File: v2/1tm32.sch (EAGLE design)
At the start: 48 parts, among them IC1 STM32L412RBT6P, IC2 BGM240PA32VNN3, IC3 TPS7A0333PYCHR, J2 10118192-0001LF, J3 FTSH-105-01-L-D, J4 20021321-00020C4LF, SW1 LL3301FF065QJ, U2 LD39050PU33R, Y1 8MHz, Y2 32.7KHz

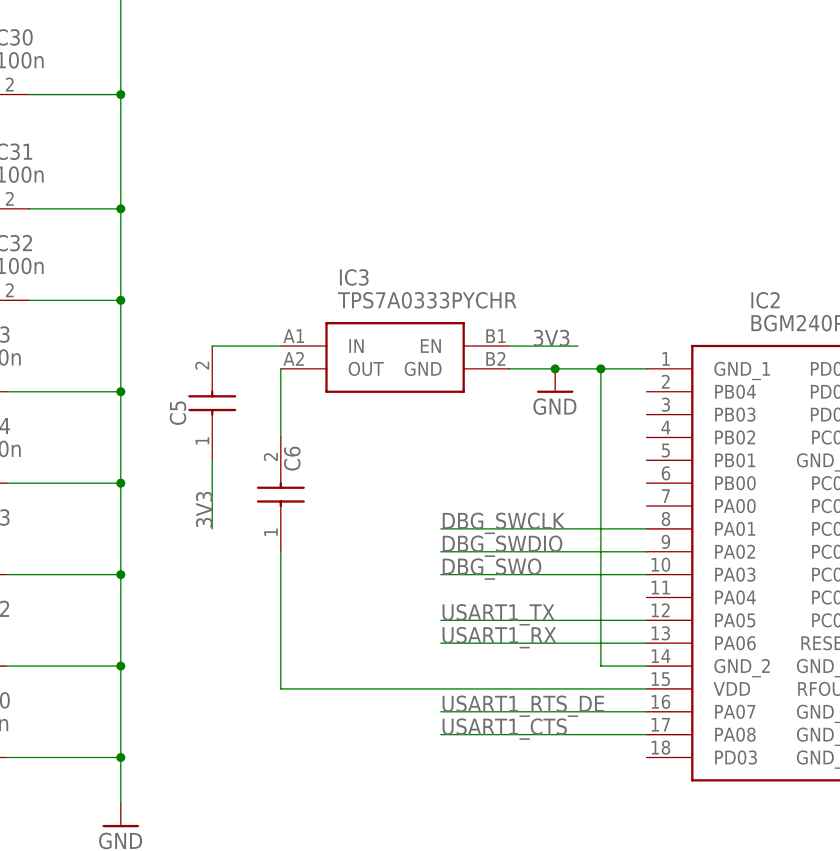
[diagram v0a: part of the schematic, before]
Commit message: changed voltage regulator
previous one caused clearance issues with the wires
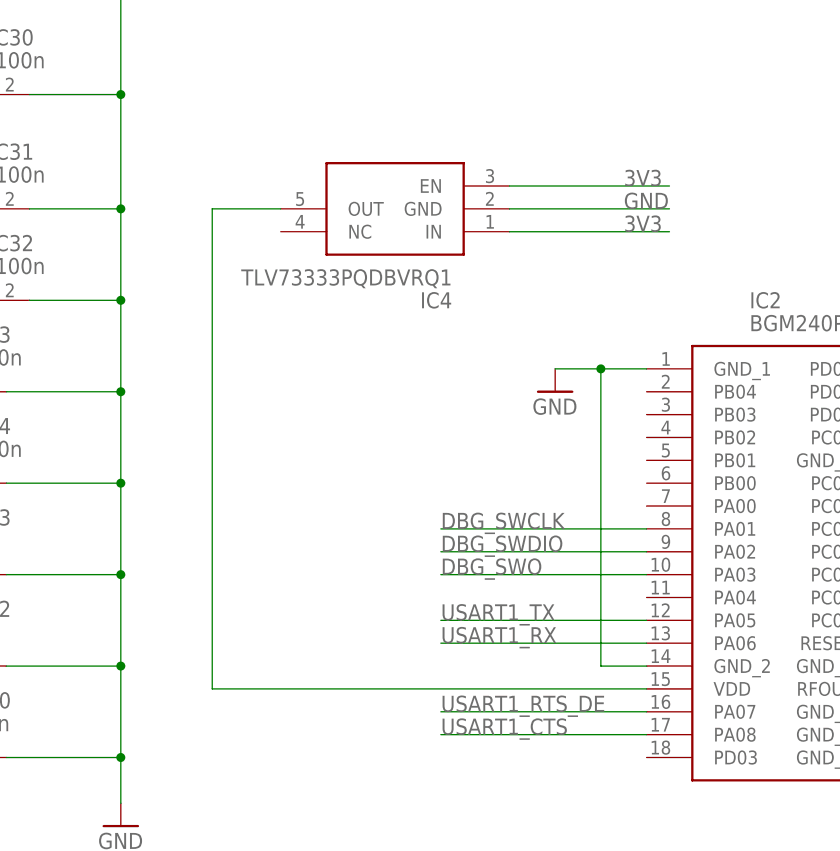
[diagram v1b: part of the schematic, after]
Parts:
- removed C5, C6: GRM219R61H105KA73D, GRM219R61H105KA73D(1u):GRM219R61H105KA73D
- removed IC3: TPS7A0333PYCHR, TPS7A0333PYCHR(volt_reg):TPS7A0333PYCHR
- added IC4: TLV73333PQDBVRQ1, TLV73333PQDBVRQ1(volt_reg2):TLV73333PQDBVRQ1
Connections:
- removed net N$1: C6.2, IC3.OUT
- removed net N$6: C5.2, IC3.IN
- net 3V3: now also IC4.EN, IC4.IN; no longer C5.1, IC3.EN
- net GND: now also IC4.GND; no longer IC3.GND
- net N$4: now also IC4.OUT; no longer C6.1
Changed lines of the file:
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@@
 <part name="R11" library="RC0805JR-0710KL" deviceset="RC0805JR-0710KL" device="" value="10K"/>
 <part name="U$2" library="RBR1L30ATE25(scho_diode)" deviceset="RBR1L30ATE25" device=""/>
-<part name="IC3" library="TPS7A0333PYCHR(volt_reg)" deviceset="TPS7A0333PYCHR" device=""/>
-<part name="C5" library="GRM219R61H105KA73D(1u)" deviceset="GRM219R61H105KA73D" device=""/>
-<part name="C6" library="GRM219R61H105KA73D(1u)" deviceset="GRM219R61H105KA73D" device=""/>
+<part name="IC4" library="TLV73333PQDBVRQ1(volt_reg2)" deviceset="TLV73333PQDBVRQ1" device=""/>
 </parts>
 <sheets>
@@
 <attribute name="VALUE" x="-150.1394" y="138.6586" size="2.0828" layer="96" ratio="6" rot="SR0"/>
 </instance>
-<instance part="IC3" gate="G$1" x="-73.66" y="-45.72" smashed="yes">
-<attribute name="NAME" x="-67.31" y="-38.1" size="1.778" layer="95" align="center-left"/>
-<attribute name="VALUE" x="-67.31" y="-40.64" size="1.778" layer="96" align="center-left"/>
-</instance>
-<instance part="C5" gate="G$1" x="-81.28" y="-58.42" smashed="yes" rot="R90">
-<attribute name="NAME" x="-85.09" y="-54.61" size="1.778" layer="95" rot="R90" align="center-left"/>
-</instance>
-<instance part="C6" gate="G$1" x="-73.66" y="-68.58" smashed="yes" rot="R90">
-<attribute name="NAME" x="-72.39" y="-59.69" size="1.778" layer="95" rot="R90" align="center-left"/>
+<instance part="IC4" gate="G$1" x="-48.26" y="-33.02" smashed="yes" rot="R180">
+<attribute name="NAME" x="-54.61" y="-40.64" size="1.778" layer="95" rot="R180" align="center-left"/>
+<attribute name="VALUE" x="-54.61" y="-38.1" size="1.778" layer="96" rot="R180" align="center-left"/>
 </instance>
 </instances>
@@
 <wire x1="-38.1" y1="-81.28" x2="-38.1" y2="-48.26" width="0.1524" layer="91"/>
 <junction x="-38.1" y="-48.26"/>
-<pinref part="IC3" gate="G$1" pin="GND"/>
-<wire x1="-48.26" y1="-48.26" x2="-43.18" y2="-48.26" width="0.1524" layer="91"/>
-<junction x="-43.18" y="-48.26"/>
 </segment>
 <segment>
@@
 <label x="124.46" y="-17.78" size="1.778" layer="95"/>
 </segment>
+<segment>
+<pinref part="IC4" gate="G$1" pin="GND"/>
+<wire x1="-48.26" y1="-30.48" x2="-30.48" y2="-30.48" width="0.1524" layer="91"/>
+<label x="-35.56" y="-30.48" size="1.778" layer="95"/>
+</segment>
 </net>
 <net name="BOOT0" class="0">
@@
 </segment>
 <segment>
-<pinref part="IC3" gate="G$1" pin="EN"/>
-<wire x1="-48.26" y1="-45.72" x2="-40.64" y2="-45.72" width="0.1524" layer="91"/>
-<label x="-45.72" y="-45.72" size="1.778" layer="95"/>
-</segment>
-<segment>
-<pinref part="C5" gate="G$1" pin="1"/>
-<wire x1="-81.28" y1="-58.42" x2="-81.28" y2="-66.04" width="0.1524" layer="91"/>
-<label x="-81.28" y="-66.04" size="1.778" layer="95" rot="R90"/>
+<pinref part="IC4" gate="G$1" pin="EN"/>
+<wire x1="-48.26" y1="-27.94" x2="-30.48" y2="-27.94" width="0.1524" layer="91"/>
+<label x="-35.56" y="-27.94" size="1.778" layer="95"/>
+</segment>
+<segment>
+<pinref part="IC4" gate="G$1" pin="IN"/>
+<wire x1="-48.26" y1="-33.02" x2="-30.48" y2="-33.02" width="0.1524" layer="91"/>
+<label x="-35.56" y="-33.02" size="1.778" layer="95"/>
 </segment>
 </net>
@@
 <segment>
 <pinref part="IC2" gate="G$1" pin="VDD"/>
-<wire x1="-73.66" y1="-83.82" x2="-33.02" y2="-83.82" width="0.1524" layer="91"/>
-<pinref part="C6" gate="G$1" pin="1"/>
-<wire x1="-73.66" y1="-68.58" x2="-73.66" y2="-83.82" width="0.1524" layer="91"/>
-</segment>
-</net>
-<net name="N$1" class="0">
-<segment>
-<pinref part="IC3" gate="G$1" pin="OUT"/>
-<pinref part="C6" gate="G$1" pin="2"/>
-<wire x1="-73.66" y1="-48.26" x2="-73.66" y2="-55.88" width="0.1524" layer="91"/>
-</segment>
-</net>
-<net name="N$6" class="0">
-<segment>
-<pinref part="IC3" gate="G$1" pin="IN"/>
-<pinref part="C5" gate="G$1" pin="2"/>
-<wire x1="-73.66" y1="-45.72" x2="-81.28" y2="-45.72" width="0.1524" layer="91"/>
-</segment>
-</net>
+<wire x1="-81.28" y1="-83.82" x2="-33.02" y2="-83.82" width="0.1524" layer="91"/>
+<pinref part="IC4" gate="G$1" pin="OUT"/>
+<wire x1="-73.66" y1="-30.48" x2="-81.28" y2="-30.48" width="0.1524" layer="91"/>
+<wire x1="-81.28" y1="-30.48" x2="-81.28" y2="-83.82" width="0.1524" layer="91"/>
+</segment>
+</net>
